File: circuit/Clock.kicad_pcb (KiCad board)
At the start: 2 copper layers, 100 x 41 mm, 14 parts

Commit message: updated to be gooderer
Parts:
- removed 10k: R, Resistor_THT:R_Axial_DIN0204_L3.6mm_D1.6mm_P2.54mm_Vertical
- removed WeMos S2 Mini: WeMos_S2_mini, wemos2:wemoss2
- added 100nF: 100nF, Capacitor_THT:C_Disc_D8.0mm_W2.5mm_P5.00mm, F.Cu at (129.5, 120.5)
- added 10kΩ: R, Resistor_THT:R_Axial_DIN0204_L3.6mm_D1.6mm_P2.54mm_Vertical, F.Cu at (135.0, 129.0)
- added U1: WeMos_S2_mini, wemos2:wemoss2, F.Cu at (103.5, 108.2)
- moved H3 161.6 mm to (160.0, 129.0)
- moved Display 90.4 mm to (120.0, 130.7), turned to 180 degrees
- moved Plus 84.5 mm to (85.4, 100.5)
- moved R2 84.2 mm to (143.4, 125.5)
- moved Triangle 83.5 mm to (140.5, 100.5)
- moved Circle 83.4 mm to (122.5, 100.5)
- moved Minus 83.2 mm to (103.0, 100.5)
- moved H1 82.7 mm to (160.0, 98.0)
- moved H2 81.6 mm to (71.0, 129.5)
- moved kibuzzard-696711A4 80.3 mm to (139.0, 108.5)
- moved kibuzzard-696745C6 80.3 mm to (139.0, 112.0)
- moved H4 53.6 mm to (71.0, 98.0)
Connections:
- net Net-(Circle1-Pin_3) renamed /Power
- Circle pad 2: Net-(Circle1-Pin_2) -> /CircleSignal
- Display pad 1: Net-(Display1-Pin_1) -> /Clock
- Display pad 2: Net-(Display1-Pin_2) -> /CS
- Display pad 3: Net-(Display1-Pin_3) -> /DisplaySignal
- Minus pad 2: Net-(Minus1-Pin_2) -> /MinusSignal
- Plus pad 2: Net-(Plus1-Pin_2) -> /PlusSignal
- R2 pad 1: Net-(U1-GPIO40) -> /PhotoresistorSignal
- Triangle pad 2: Net-(Triangle1-Pin_2) -> /TriangleSignal
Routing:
- net /Ground: track 208.8 -> 0.00 mm
- net /PhotoresistorSignal: track 0.00 -> 57.0 mm
- net /TriangleSignal: track 0.00 -> 51.4 mm
- net Net-(U1-GPIO40): track 50.1 -> 0.00 mm
- net Net-(Triangle1-Pin_2): track 45.7 -> 0.00 mm
- net /Power: track 131.4 -> 175.7 mm
- net /CircleSignal: track 0.00 -> 35.9 mm
- net /DisplaySignal: track 0.00 -> 35.3 mm
- net Net-(Circle1-Pin_2): track 29.8 -> 0.00 mm
- net /CS: track 0.00 -> 28.8 mm
- net /Clock: track 0.00 -> 26.1 mm
- net Net-(Display1-Pin_2): track 24.8 -> 0.00 mm
- net Net-(Display1-Pin_1): track 22.0 -> 0.00 mm
- net Net-(Display1-Pin_3): track 21.5 -> 0.00 mm
- net /MinusSignal: track 0.00 -> 18.3 mm
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- added copper zone on B.Cu, net /Ground
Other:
- board size 100 x 41 mm -> 100 x 42 mm
- board text added: "VCC GND DIN CS CLK"
- board text added: "WeMos S2 Mini"
- board text removed: "CLK CS DIN GND VCC"

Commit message: rev 1.0 of pcb
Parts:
- removed kibuzzard-696711A4: G***, kibuzzard-696711A4
- added kibuzzard-696B2912: G***, kibuzzard-696B2912, F.Cu at (139.0, 108.0)
- GL5516 LDR: renamed from R2
- moved 100nF 1.50 mm to (129.5, 119.0)
- moved Display 1.50 mm to (120.0, 129.2)
- moved U1 1.18 mm to (103.5, 107.0)
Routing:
- net /PhotoresistorSignal: track 57.0 -> 58.3 mm
- net /PlusSignal: track 8.86 -> 7.68 mm
- net /MinusSignal: track 18.3 -> 17.1 mm
- net /CircleSignal: track 35.9 -> 34.7 mm
- net /TriangleSignal: track 51.4 -> 50.2 mm
- net /DisplaySignal: track 35.3 -> 36.5 mm
- net /Power: track 175.7 -> 176.3 mm

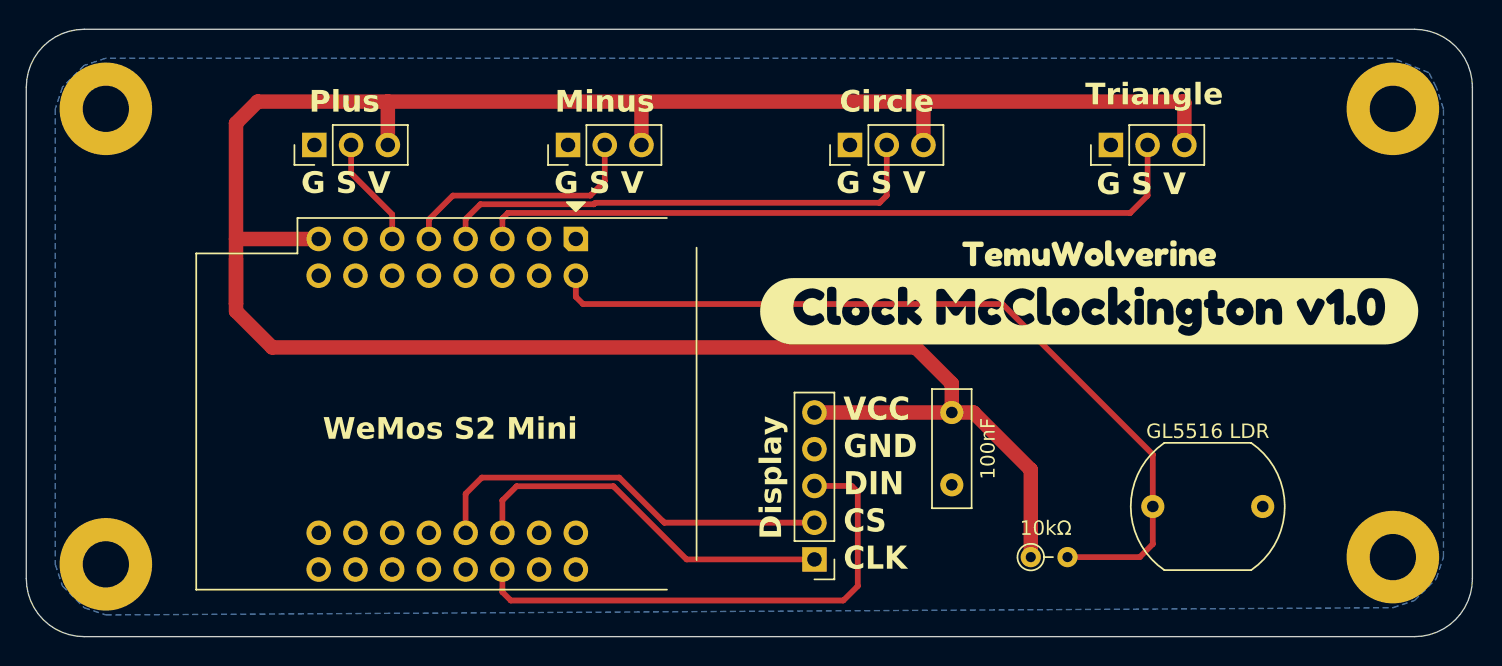
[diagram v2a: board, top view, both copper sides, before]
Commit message: Update Clock PCB nets & footprints
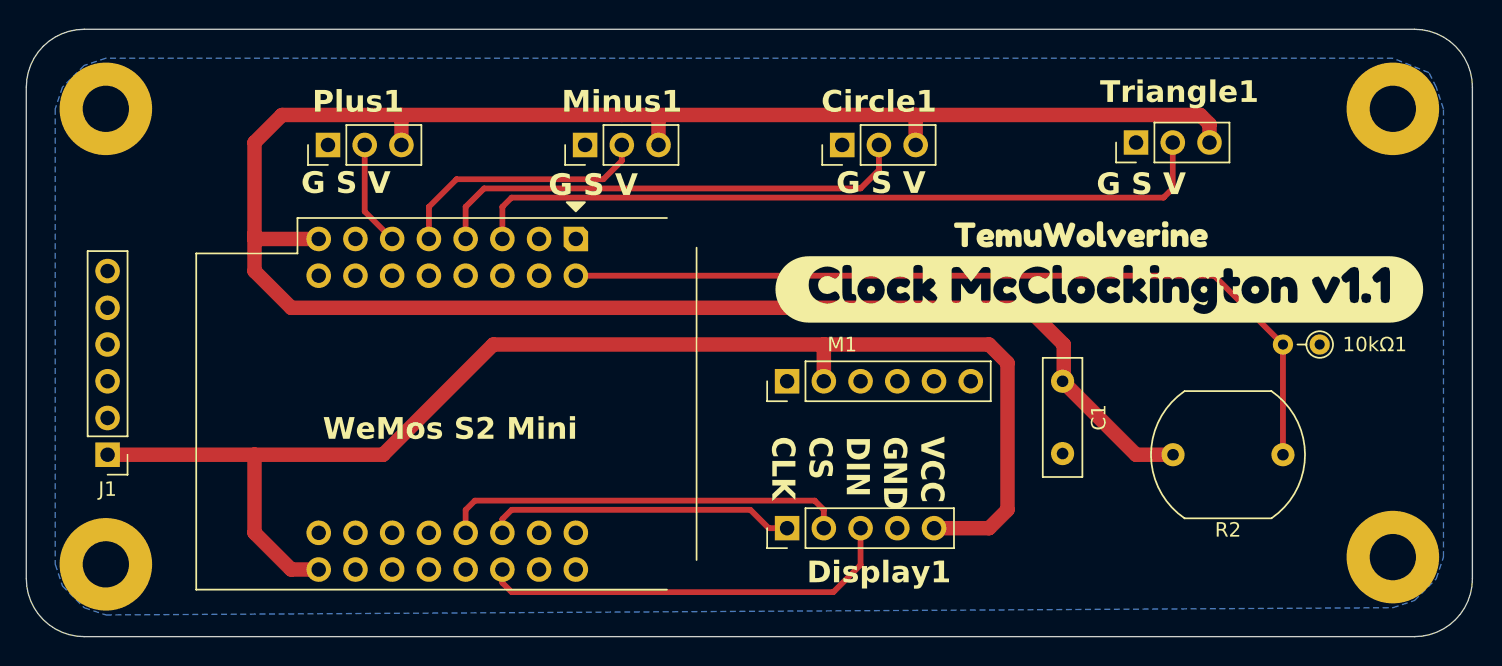
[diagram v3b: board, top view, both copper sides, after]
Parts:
- removed kibuzzard-696745C6: G***, kibuzzard-696745C6
- added J1: Conn_01x06_Pin, Connector_PinHeader_2.54mm:PinHeader_1x06_P2.54mm_Vertical, F.Cu at (71.1, 121.9)
- added M1: ~, Library:INMP441, F.Cu at (118.1, 116.8)
- added kibuzzard-697FC5C7: G***, kibuzzard-697FC5C7, F.Cu at (139.7, 110.5)
- R2: renamed from GL5516 LDR
- moved 10kΩ1 24.8 mm to (154.9, 114.3), turned to 180 degrees
- moved R2 9.69 mm to (152.4, 121.9), turned to 180 degrees
- moved C1 7.96 mm to (137.2, 116.8)
- moved Display1 2.87 mm to (118.1, 127.0), turned to 90 degrees
- moved Triangle1 1.75 mm to (142.2, 100.3)
- moved kibuzzard-696B2912 1.44 mm to (138.4, 106.7)
- moved Minus1 1.18 mm to (104.1, 100.5)
- moved Plus1 0.94 mm to (86.4, 100.5)
- moved Circle1 0.54 mm to (121.9, 100.5)
- renumbered 10kΩ to 10kΩ1, 100nF to C1, Circle to Circle1, Display to Display1, Minus to Minus1, Plus to Plus1, Triangle to Triangle1
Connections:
- net /CircleSignal renamed circle
- net /MinusSignal renamed MinusSignal
- net /PlusSignal renamed PlusSignal
- net /TriangleSignal renamed triangle
- 10kΩ1 pad 1: /Power -> GND
- C1 pad 1: /Power -> +3V3
- C1 pad 2: /Ground -> GND
- Circle1 pad 1: /Ground -> GND
- Circle1 pad 3: /Power -> +3V3
- Display1 pad 4: /Ground -> GND
- Display1 pad 5: /Power -> +5V
- H1 pad 1: /Ground -> GND
- H2 pad 1: /Ground -> GND
- H3 pad 1: /Ground -> GND
- H4 pad 1: /Ground -> GND
- Minus1 pad 1: /Ground -> GND
- Minus1 pad 3: /Power -> +3V3
- Plus1 pad 1: /Ground -> GND
- Plus1 pad 3: /Power -> +3V3
- R2 pad 2: /Ground -> +3V3
- Triangle1 pad 1: /Ground -> GND
- Triangle1 pad 3: /Power -> +3V3
- U1 pad 10: /Ground -> GND
- U1 pad 26: /Ground -> GND
- U1 pad 8: /Power -> +3V3
- U1 pad 9: unconnected-(U1-VBUS-Pad9) -> +5V
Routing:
- net /Power: track 176.3 -> 0.00 mm
- net +3V3: track 0.00 -> 158.6 mm
- net +5V: track 0.00 -> 95.1 mm
- net /DisplaySignal: track 36.5 -> 29.3 mm
- net /Clock: track 26.3 -> 21.4 mm
- net triangle: track 50.2 -> 52.3 mm
- net circle: track 34.7 -> 33.6 mm
- net MinusSignal: track 17.1 -> 18.0 mm
- added copper zone on B.Cu, net GND
- removed copper zone on B.Cu, net /Ground

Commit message: updated pcb
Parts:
- added C2: 100nF, Capacitor_THT:C_Disc_D8.0mm_W2.5mm_P5.00mm, F.Cu at (51.4, 65.8)
- added U2: ESP32-S3-ZERO, waveshare:MODULE_ESP32-S3-ZERO, F.Cu at (39.4, 77.5)
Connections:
- net /CS renamed CS
- net /Clock renamed Clock
- net /DisplaySignal renamed DisplaySignal
- net /PhotoresistorSignal renamed PhotoresistorSignal
- M1 pad SCK: unconnected-(M1-PadSCK) -> SCK
- M1 pad SD: unconnected-(M1-PadSD) -> SD
- M1 pad WS: unconnected-(M1-PadWS) -> WS

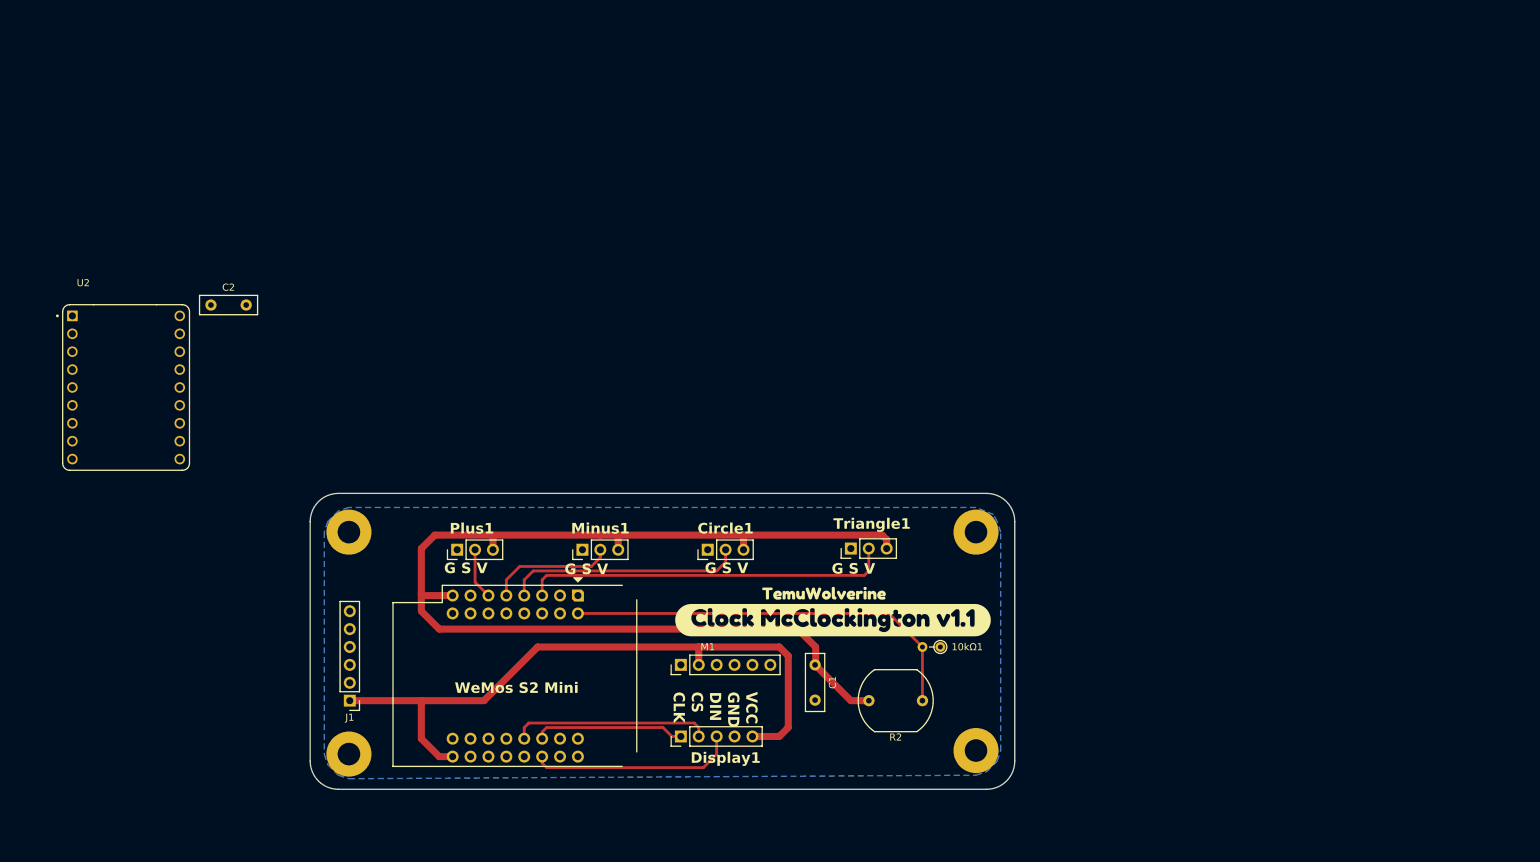
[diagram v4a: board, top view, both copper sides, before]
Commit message: ESPHome config now works - needed two I2S channels for input/output. Updated circuit design to reflect this, and better designed PCB/layout with updated ESPS3-zero footprint/symbol
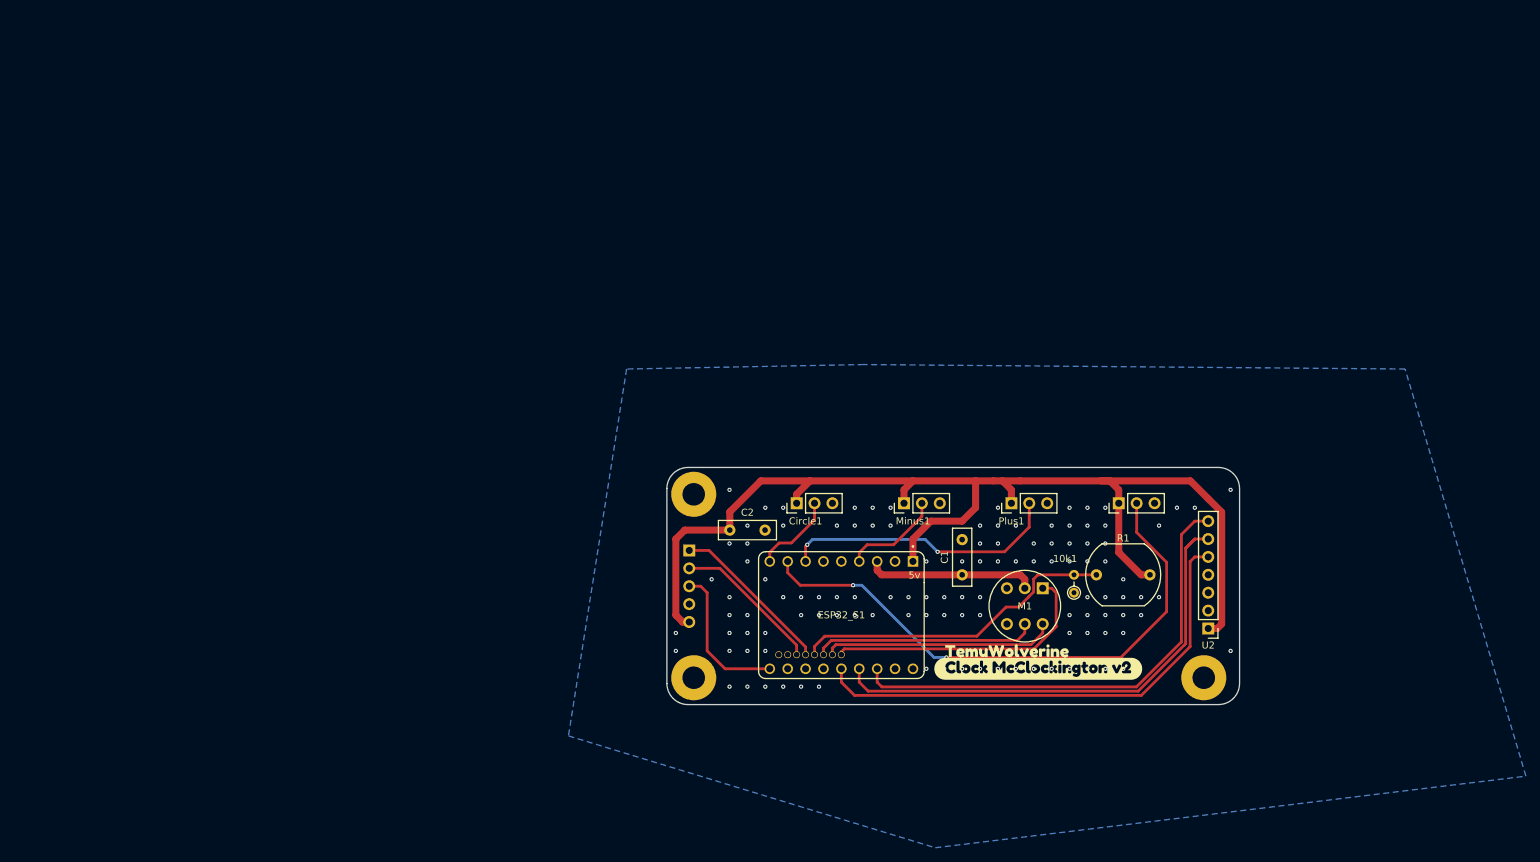
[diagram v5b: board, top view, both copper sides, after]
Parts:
- removed 10kΩ1: R, Resistor_THT:R_Axial_DIN0204_L3.6mm_D1.6mm_P2.54mm_Vertical
- removed H4: MountingHole_Pad, MountingHole:MountingHole_3.2mm_M3_Pad
- removed J1: Conn_01x06_Pin, Connector_PinHeader_2.54mm:PinHeader_1x06_P2.54mm_Vertical
- removed R2: LDR03, OptoDevice:R_LDR_10x8.5mm_P7.6mm_Vertical
- removed U1: WeMos_S2_mini, wemos2:wemoss2
- removed kibuzzard-697FC5C7: G***, kibuzzard-697FC5C7
- added 10k1: R, Resistor_THT:R_Axial_DIN0204_L3.6mm_D1.6mm_P2.54mm_Vertical, F.Cu at (173.9, 106.6)
- added ESP32_S1: ~, PaulsCoolKicadLibrary:MODULE_ESP32-S3-ZERO, F.Cu at (140.9, 109.8)
- added R1: LDR03, OptoDevice:R_LDR_10x8.5mm_P7.6mm_Vertical, F.Cu at (177.1, 104.1)
- added kibuzzard-69B23704: G***, kibuzzard-69B23704, F.Cu at (168.8, 117.4)
- Circle1, Minus1, Plus1, Triangle1: value Conn_01x03_Pin -> TPP223
- Display1: footprint Connector_PinHeader_2.54mm:PinHeader_1x05_P2.54mm_Vertical -> Connector_PinSocket_2.54mm:PinSocket_1x05_P2.54mm_Vertical; moved to B.Cu
- M1: footprint Library:INMP441 -> PaulsCoolKicadLibrary:INMP441
- U2: value ESP32-S3-ZERO -> Max98357; footprint waveshare:MODULE_ESP32-S3-ZERO -> Connector_PinHeader_2.54mm:PinHeader_1x07_P2.54mm_Vertical
- moved U2 157.4 mm to (193.0, 111.7), turned to 180 degrees
- moved C2 80.3 mm to (125.1, 97.7)
- moved Plus1 78.9 mm to (165.0, 93.9)
- moved M1 52.5 mm to (169.5, 106.0), turned to -90 degrees
- moved H2 50.1 mm to (119.9, 118.7)
- moved Minus1 46.1 mm to (149.8, 93.9)
- moved H1 40.4 mm to (119.9, 92.6)
- moved Triangle1 38.6 mm to (180.3, 93.9)
- moved H3 33.9 mm to (192.3, 118.7)
- moved kibuzzard-696B2912 27.2 mm to (164.4, 114.9)
- moved Display1 26.4 mm to (119.3, 100.6), turned to 180 degrees
- moved C1 24.5 mm to (158.0, 104.1), turned to 90 degrees
- moved Circle1 14.2 mm to (134.5, 93.9)
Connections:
- Circle1 pad 1: GND -> +5V
- Circle1 pad 3: +3V3 -> GND
- M1 pad SD: SD -> MIC_DIN
- M1 pad VDD: +5V -> +3V3
- Minus1 pad 1: GND -> +5V
- Minus1 pad 3: +3V3 -> GND
- Plus1 pad 1: GND -> +5V
- Plus1 pad 3: +3V3 -> GND
- Triangle1 pad 1: GND -> +5V
- Triangle1 pad 3: +3V3 -> GND
- U2 pad 1: unconnected-(U2-GP1-Pad1) -> +5V
- U2 pad 2: Clock -> GND
- U2 pad 3: CS -> unconnected-(U2-Pin_3-Pad3)
- U2 pad 4: DisplaySignal -> GND
- U2 pad 5: unconnected-(U2-GP5-Pad5) -> SPK_DOUT
- U2 pad 6: triangle -> BLCK
- U2 pad 7: circle -> LRCK
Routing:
- net +3V3: track 158.6 -> 24.0 mm
- net BLCK: track 0.00 -> 70.6 mm
- net SPK_DOUT: track 0.00 -> 70.0 mm
- net LRCK: track 0.00 -> 67.8 mm
- net +5V: track 95.1 -> 162.2 mm
- net MIC_DIN: track 0.00 -> 39.4 mm
- net SCK: track 0.00 -> 32.9 mm
- net PlusSignal: track 7.29 -> 39.8 mm, vias 0 -> 2
- net WS: track 0.00 -> 31.7 mm
- net triangle: track 52.3 -> 80.2 mm, vias 0 -> 2
- net circle: track 33.6 -> 11.9 mm
- net PhotoresistorSignal: track 58.5 -> 46.5 mm
- net DisplaySignal: track 29.3 -> 21.1 mm
- net CS: track 28.2 -> 21.1 mm
- net MinusSignal: track 18.0 -> 14.1 mm
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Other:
- board size 100 x 42 mm -> 81.3 x 33.7 mm
- board text removed: "G S V"
- board text removed: "VCC GND DIN CS CLK"
- board text removed: "WeMos S2 Mini"

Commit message: more tweaks
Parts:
- Display1: moved to F.Cu
- moved kibuzzard-696B2912 24.5 mm to (187.9, 107.9), turned to 90 degrees
- moved C1 12.0 mm to (169.6, 100.9), turned to 45 degrees
- moved 10k1 9.66 mm to (179.5, 114.5)
- moved R1 7.27 mm to (182.3, 109.1), turned to 90 degrees
- moved C2 4.54 mm to (126.8, 93.5), turned to -45 degrees
- moved M1 4.21 mm to (173.7, 105.6)
- moved ESP32_S1 3.56 mm to (137.3, 109.8)
- turned Display1 to 0 degrees
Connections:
- ESP32_S1 pad 40: PhotoresistorSignal -> MIC_DIN
- ESP32_S1 pad 41: WS -> PhotoresistorSignal
- ESP32_S1 pad 42: SCK -> WS
- ESP32_S1 pad 45: MIC_DIN -> SCK
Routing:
- net +3V3: track 24.0 -> 35.3 mm
- net triangle: track 80.2 -> 87.9 mm
- net MIC_DIN: track 39.4 -> 46.8 mm
- net PhotoresistorSignal: track 46.5 -> 52.7 mm
- net WS: track 31.7 -> 37.7 mm
- net SCK: track 32.9 -> 38.4 mm
- net DisplaySignal: track 21.1 -> 16.6 mm
- net MinusSignal: track 14.1 -> 17.8 mm
- net BLCK: track 70.6 -> 74.2 mm
- net circle: track 11.9 -> 15.4 mm
- net LRCK: track 67.8 -> 71.3 mm
- net SPK_DOUT: track 70.0 -> 73.2 mm
- net PlusSignal: track 39.8 -> 43.0 mm
- net Clock: track 23.3 -> 25.7 mm
- net +5V: track 162.2 -> 160.1 mm
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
